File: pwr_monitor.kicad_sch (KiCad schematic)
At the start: 2 parts

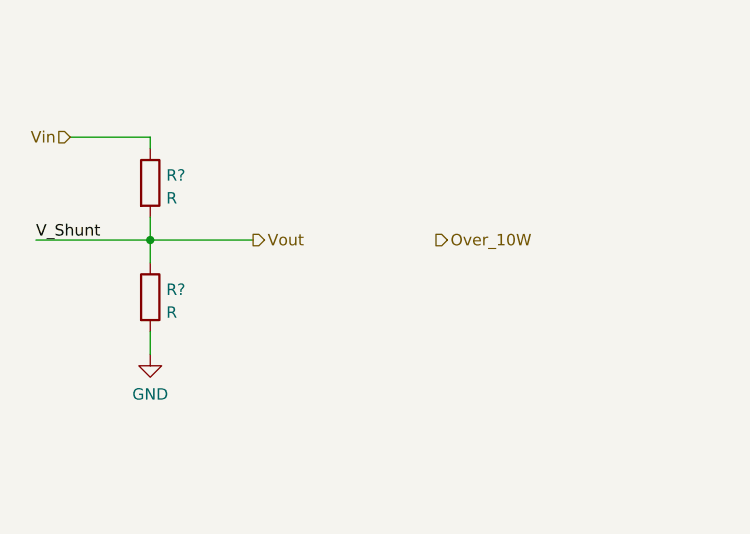
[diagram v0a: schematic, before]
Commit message: Add op-amp for power monitoring
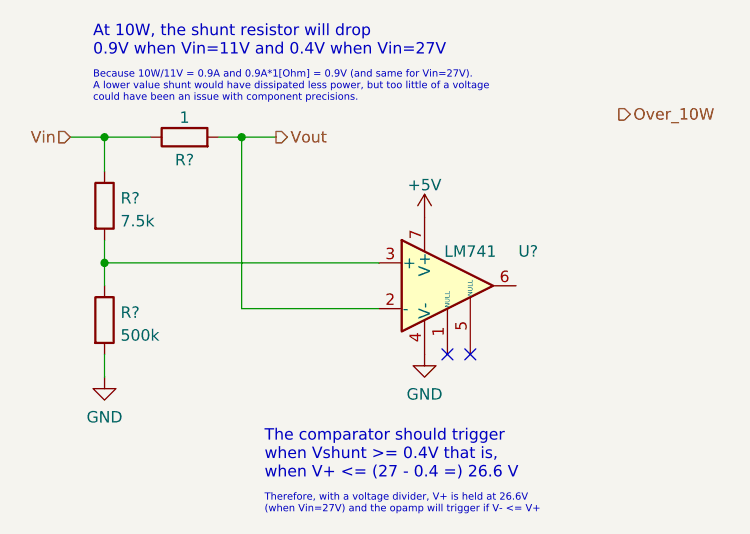
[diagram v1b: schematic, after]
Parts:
- removed R?: R, symbol Device:R
- added R?: 7.5k, symbol Device:R
- added R?: 500k, symbol Device:R
- added U?: LM741, symbol Amplifier_Operational:LM741
- R?: value R -> 1
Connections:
- net GND: now also R?.2, U?.4 (V-)
- net Vin: now also R?.1
- net Vout: now also U?.2 (-)
- new net: R?.1, R?.2, U?.3 (+)
- new net +5V: U?.7 (V+)
- no-connect marks 0 -> 2
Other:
- note added: "At 10W, the shunt resistor will drop 0.9V when Vin=11V and 0.4V when Vin=27V"
- note added: "Because 10W/11V = 0.9A and 0.9A*1[Ohm] = 0.9V (and same for Vin=27V). A lower value shunt would have dissipated less power, but too little of a voltage could have been an issue with component precisions."
- note added: "The comparator should trigger when Vshunt >= 0.4V that is, when V+ <= (27 - 0.4 =) 26.6 V"
- note added: "Therefore, with a voltage divider, V+ is held at 26.6V (when Vin=27V) and the opamp will trigger if V- <= V+"
- moved on the sheet: R?
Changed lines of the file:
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@@
 (kicad_sch (version 20211123) (generator eeschema)
   (paper "A4")
-  (junction (at 74.93 86.36) (diameter 0) (color 0 0 0 0)
+  (junction (at 69.85 74.93) (diameter 0) (color 0 0 0 0)
   )
-  (wire (pts (xy 74.93 86.36) (xy 74.93 88.9))
+  (junction (at 85.09 74.93) (diameter 0) (color 0 0 0 0)
+  )
+  (junction (at 69.85 88.9) (diameter 0) (color 0 0 0 0)
+  )
+  (no_connect (at 107.95 99.06))
+  (no_connect (at 110.49 99.06))
+  (wire (pts (xy 69.85 88.9) (xy 100.33 88.9))
     (stroke (width 0) (type default) (color 0 0 0 0))
   )
-  (wire (pts (xy 74.93 96.52) (xy 74.93 99.06))
+  (wire (pts (xy 69.85 86.36) (xy 69.85 88.9))
     (stroke (width 0) (type default) (color 0 0 0 0))
   )
-  (wire (pts (xy 74.93 74.93) (xy 74.93 76.2))
+  (wire (pts (xy 85.09 74.93) (xy 85.09 93.98))
     (stroke (width 0) (type default) (color 0 0 0 0))
   )
-  (wire (pts (xy 62.23 86.36) (xy 74.93 86.36))
+  (wire (pts (xy 69.85 74.93) (xy 69.85 78.74))
     (stroke (width 0) (type default) (color 0 0 0 0))
   )
-  (wire (pts (xy 74.93 83.82) (xy 74.93 86.36))
+  (wire (pts (xy 82.55 74.93) (xy 85.09 74.93))
     (stroke (width 0) (type default) (color 0 0 0 0))
   )
-  (wire (pts (xy 66.04 74.93) (xy 74.93 74.93))
+  (wire (pts (xy 69.85 88.9) (xy 69.85 91.44))
     (stroke (width 0) (type default) (color 0 0 0 0))
   )
-  (wire (pts (xy 74.93 86.36) (xy 86.36 86.36))
+  (wire (pts (xy 66.04 74.93) (xy 69.85 74.93))
     (stroke (width 0) (type default) (color 0 0 0 0))
   )
-  (label "V_Shunt" (at 62.23 86.36 0)
+  (wire (pts (xy 69.85 74.93) (xy 74.93 74.93))
+    (stroke (width 0) (type default) (color 0 0 0 0))
+  )
+  (wire (pts (xy 85.09 93.98) (xy 100.33 93.98))
+    (stroke (width 0) (type default) (color 0 0 0 0))
+  )
+  (wire (pts (xy 69.85 99.06) (xy 69.85 101.6))
+    (stroke (width 0) (type default) (color 0 0 0 0))
+  )
+  (wire (pts (xy 85.09 74.93) (xy 88.9 74.93))
+    (stroke (width 0) (type default) (color 0 0 0 0))
+  )
+  (text "Because 10W/11V = 0.9A and 0.9A*1[Ohm] = 0.9V (and same for Vin=27V).\nA lower value shunt would have dissipated less power, but too little of a voltage\ncould have been an issue with component precisions."
+    (at 68.58 71.12 0)
+    (effects (font (size 0.8 0.8)) (justify left bottom))
+  )
+  (text "At 10W, the shunt resistor will drop\n0.9V when Vin=11V and 0.4V when Vin=27V"
+    (at 68.58 66.04 0)
     (effects (font (size 1.27 1.27)) (justify left bottom))
   )
-  (hierarchical_label "Vout" (shape output) (at 86.36 86.36 0)
+  (text "The comparator should trigger\nwhen Vshunt >= 0.4V that is,\nwhen V+ <= (27 - 0.4 =) 26.6 V"
+    (at 87.63 113.03 0)
+    (effects (font (size 1.27 1.27)) (justify left bottom))
+  )
+  (text "Therefore, with a voltage divider, V+ is held at 26.6V\n(when Vin=27V) and the opamp will trigger if V- <= V+"
+    (at 87.63 116.84 0)
+    (effects (font (size 0.8 0.8)) (justify left bottom))
+  )
+  (hierarchical_label "Vout" (shape output) (at 88.9 74.93 0)
     (effects (font (size 1.27 1.27)) (justify left))
   )
@@
     (effects (font (size 1.27 1.27)) (justify right))
   )
-  (hierarchical_label "Over_10W" (shape output) (at 106.68 86.36 0)
+  (hierarchical_label "Over_10W" (shape output) (at 127 72.39 0)
     (effects (font (size 1.27 1.27)) (justify left))
   )
-  (symbol (lib_id "Device:R") (at 74.93 92.71 0) (unit 1)
+  (symbol (lib_id "Device:R") (at 69.85 82.55 0) (unit 1)
     (in_bom yes) (on_board yes) (fields_autoplaced)
-    (property "Reference" "R?" (id 0) (at 76.708 91.8753 0)
+    (property "Reference" "R?" (id 0) (at 71.628 81.7153 0)
       (effects (font (size 1.27 1.27)) (justify left))
     )
-    (property "Value" "R" (id 1) (at 76.708 94.4122 0)
+    (property "Value" "7.5k" (id 1) (at 71.628 84.2522 0)
       (effects (font (size 1.27 1.27)) (justify left))
     )
-    (property "Footprint" "" (id 2) (at 73.152 92.71 90)
+    (property "Footprint" "" (id 2) (at 68.072 82.55 90)
       (effects (font (size 1.27 1.27)) hide)
     )
-    (property "Datasheet" "~" (id 3) (at 74.93 92.71 0)
+    (property "Datasheet" "~" (id 3) (at 69.85 82.55 0)
       (effects (font (size 1.27 1.27)) hide)
     )
@@
     (pin "2")
   )
-  (symbol (lib_id "Device:R") (at 74.93 80.01 0) (unit 1)
+  (symbol (lib_id "Amplifier_Operational:LM741") (at 107.95 91.44 0) (unit 1)
+    (in_bom yes) (on_board yes)
+    (property "Reference" "U?" (id 0) (at 116.9254 87.6133 0))
+    (property "Value" "LM741" (id 1) (at 110.49 87.63 0))
+    (property "Footprint" "" (id 2) (at 109.22 90.17 0)
+      (effects (font (size 1.27 1.27)) hide)
+    )
+    (property "Datasheet" "http://www.ti.com/lit/ds/symlink/lm741.pdf" (id 3) (at 111.76 87.63 0)
+      (effects (font (size 1.27 1.27)) hide)
+    )
+    (pin "1")
+    (pin "2")
+    (pin "3")
+    (pin "4")
+    (pin "5")
+    (pin "6")
+    (pin "7")
+    (pin "8")
+  )
+  (symbol (lib_id "Device:R") (at 69.85 95.25 0) (unit 1)
     (in_bom yes) (on_board yes) (fields_autoplaced)
-    (property "Reference" "R?" (id 0) (at 76.708 79.1753 0)
+    (property "Reference" "R?" (id 0) (at 71.628 94.4153 0)
       (effects (font (size 1.27 1.27)) (justify left))
     )
-    (property "Value" "R" (id 1) (at 76.708 81.7122 0)
+    (property "Value" "500k" (id 1) (at 71.628 96.9522 0)
       (effects (font (size 1.27 1.27)) (justify left))
     )
-    (property "Footprint" "" (id 2) (at 73.152 80.01 90)
+    (property "Footprint" "" (id 2) (at 68.072 95.25 90)
       (effects (font (size 1.27 1.27)) hide)
     )
-    (property "Datasheet" "~" (id 3) (at 74.93 80.01 0)
+    (property "Datasheet" "~" (id 3) (at 69.85 95.25 0)
       (effects (font (size 1.27 1.27)) hide)
     )
@@
     (pin "2")
   )
-  (symbol (lib_id "power:GND") (at 74.93 99.06 0) (unit 1)
+  (symbol (lib_id "power:GND") (at 69.85 101.6 0) (unit 1)
     (in_bom yes) (on_board yes) (fields_autoplaced)
-    (property "Reference" "#PWR?" (id 0) (at 74.93 105.41 0)
+    (property "Reference" "#PWR?" (id 0) (at 69.85 107.95 0)
       (effects (font (size 1.27 1.27)) hide)
     )
-    (property "Value" "GND" (id 1) (at 74.93 103.5034 0))
-    (property "Footprint" "" (id 2) (at 74.93 99.06 0)
+    (property "Value" "GND" (id 1) (at 69.85 106.0434 0))
+    (property "Footprint" "" (id 2) (at 69.85 101.6 0)
       (effects (font (size 1.27 1.27)) hide)
     )
-    (property "Datasheet" "" (id 3) (at 74.93 99.06 0)
+    (property "Datasheet" "" (id 3) (at 69.85 101.6 0)
       (effects (font (size 1.27 1.27)) hide)
     )
+    (pin "1")
+  )
+  (symbol (lib_id "Device:R") (at 78.74 74.93 90) (unit 1)
+    (in_bom yes) (on_board yes)
+    (property "Reference" "R?" (id 0) (at 78.74 77.47 90))
+    (property "Value" "1" (id 1) (at 78.74 72.7511 90))
+    (property "Footprint" "" (id 2) (at 78.74 76.708 90)
+      (effects (font (size 1.27 1.27)) hide)
+    )
+    (property "Datasheet" "~" (id 3) (at 78.74 74.93 0)
+      (effects (font (size 1.27 1.27)) hide)
+    )
+    (pin "1")
+    (pin "2")
+  )
+  (symbol (lib_id "power:GND") (at 105.41 99.06 0) (unit 1)
+    (in_bom yes) (on_board yes) (fields_autoplaced)
+    (property "Reference" "#PWR?" (id 0) (at 105.41 105.41 0)
+      (effects (font (size 1.27 1.27)) hide)
+    )
+    (property "Value" "GND" (id 1) (at 105.41 103.5034 0))
+    (property "Footprint" "" (id 2) (at 105.41 99.06 0)
+      (effects (font (size 1.27 1.27)) hide)
+    )
+    (property "Datasheet" "" (id 3) (at 105.41 99.06 0)
+      (effects (font (size 1.27 1.27)) hide)
+    )
+    (pin "1")
+  )
+  (symbol (lib_id "power:+5V") (at 105.41 83.82 0) (unit 1)
+    (in_bom yes) (on_board yes) (fields_autoplaced)
+    (property "Reference" "#PWR?" (id 0) (at 105.41 87.63 0)
+      (effects (font (size 1.27 1.27)) hide)
+    )
+    (property "Value" "+5V" (id 1) (at 105.41 80.2442 0))
+    (property "Footprint" "" (id 2) (at 105.41 83.82 0)
+      (effects (font (size 1.27 1.27)) hide)
+    )
+    (property "Datasheet" "" (id 3) (at 105.41 83.82 0)
+      (effects (font (size 1.27 1.27)) hide)
+    )

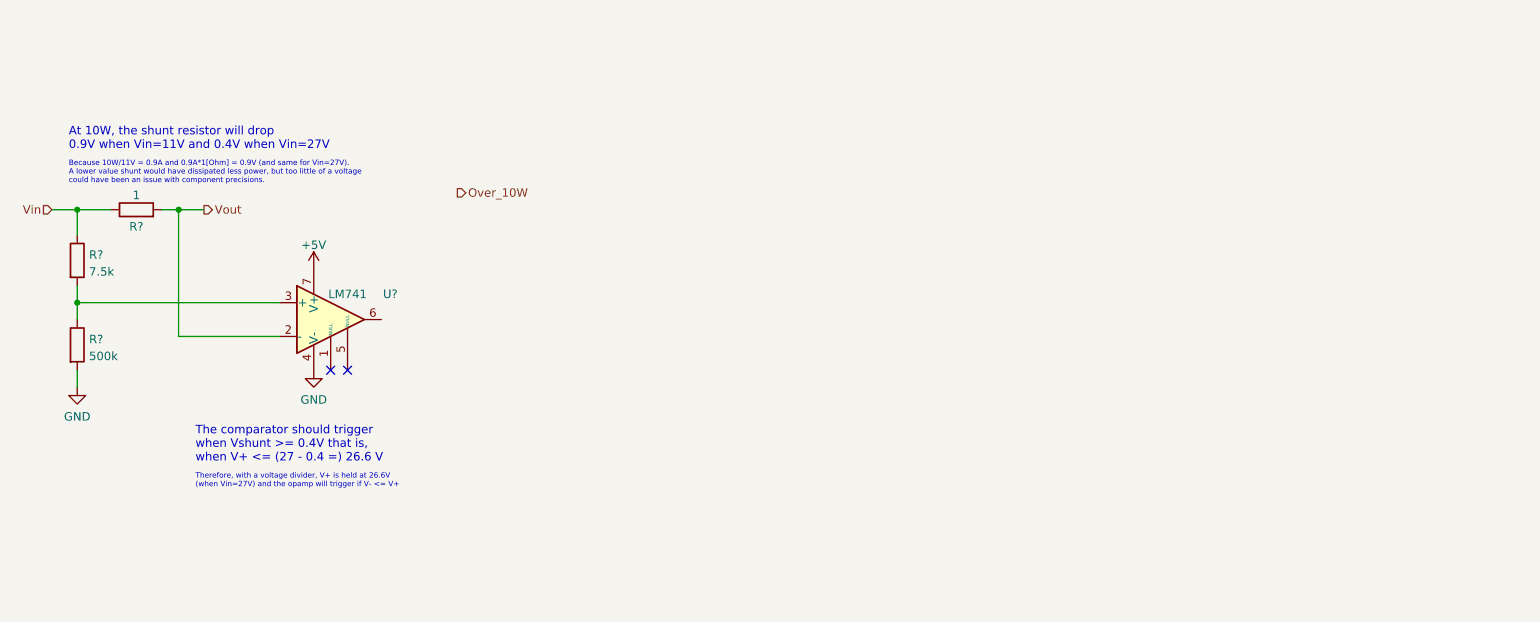
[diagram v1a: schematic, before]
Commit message: Add NE555 to blink LED at 3.5Hz
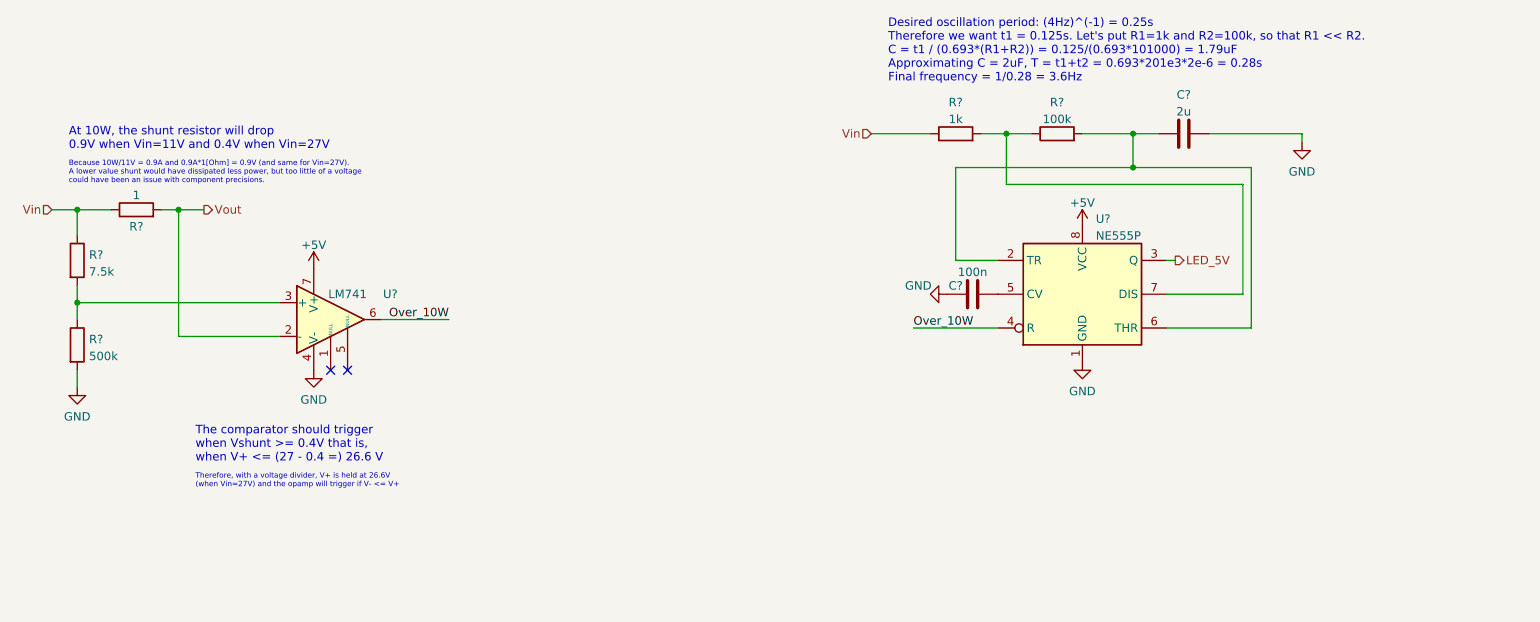
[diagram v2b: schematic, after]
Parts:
- added C?: 2u, symbol Device:C
- added C?: 100n, symbol Device:C
- added R?: 100k, symbol Device:R
- added R?: 1k, symbol Device:R
- added U?: NE555P, Package_DIP:DIP-8_W7.62mm, symbol Timer:NE555P
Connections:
- net +5V: now also U?.8 (VCC)
- net GND: now also C?.2, C?.2, U?.1 (GND)
- net Over_10W: now also U?.6, U?.4 (R)
- net Vin: now also R?.1
- new net: C?.1, R?.2, U?.2 (TR), U?.6 (THR)
- new net: R?.1, R?.2, U?.7 (DIS)
- new net: C?.1, U?.5 (CV)
- new net LED_5V: U?.3 (Q)
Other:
- note added: "Desired oscillation period: (4Hz)^(-1) = 0.25s Therefore we want t1 = 0.125s. Let's put R1=1k and R2=100k, so that R1 << R2. C = t1 / (0.693*(R1+R2)) = 0.125/(0.693*101000) = 1.79uF Approximating C = 2uF, T = t1+t2 = 0.693*201e3*2e-6 = 0.28s Final frequency = 1/0.28 = 3.6Hz"

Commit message: Finish power monitor
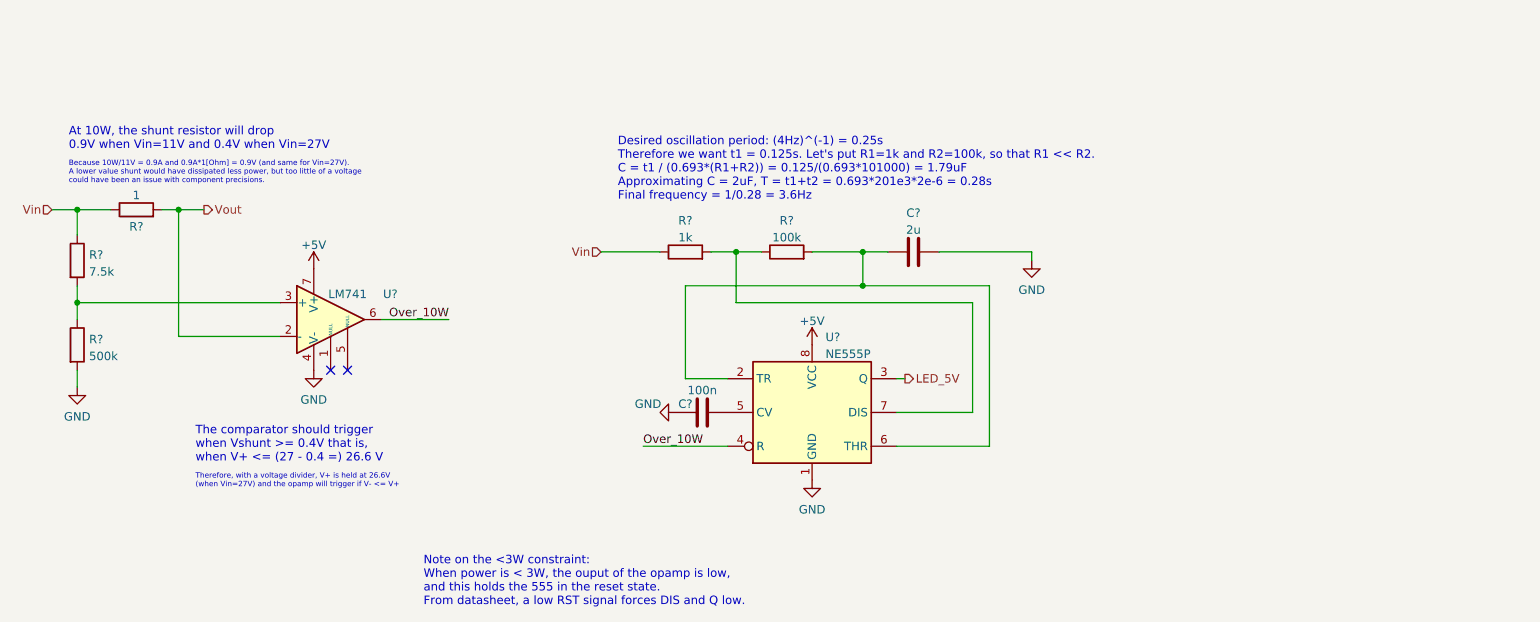
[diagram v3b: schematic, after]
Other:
- note added: "Note on the <3W constraint: When power is < 3W, the ouput of the opamp is low, and this holds the 555 in the reset state. From datasheet, a low RST signal forces DIS and Q low."
- moved on the sheet: C?, R?, U?
